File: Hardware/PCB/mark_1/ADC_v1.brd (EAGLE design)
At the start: 52.1 x 49.5 mm, 18 parts, among them IC1 MCP3424, IC2 MCP23017SO, Q1 IRLML6402, Q2 IRLML6402, Q3 IRLML6402, Q4 IRLML6402

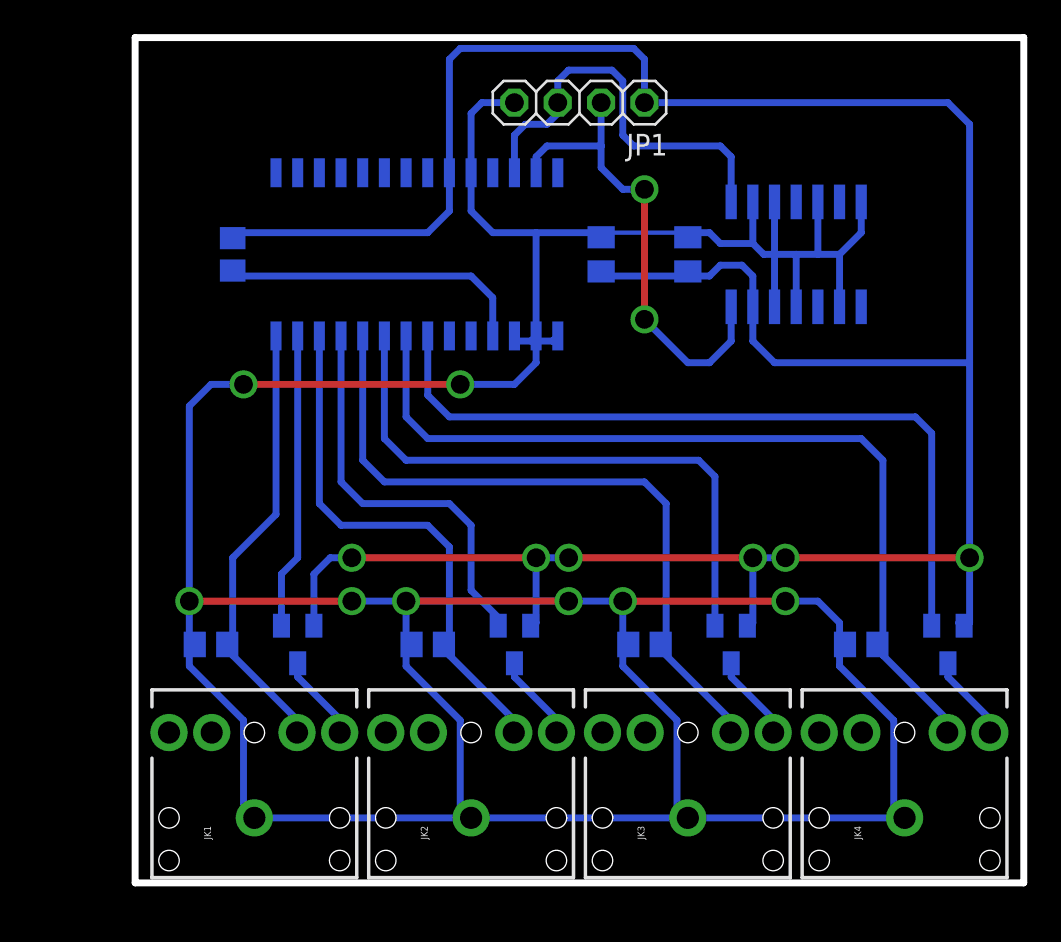
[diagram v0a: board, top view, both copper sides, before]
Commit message: 
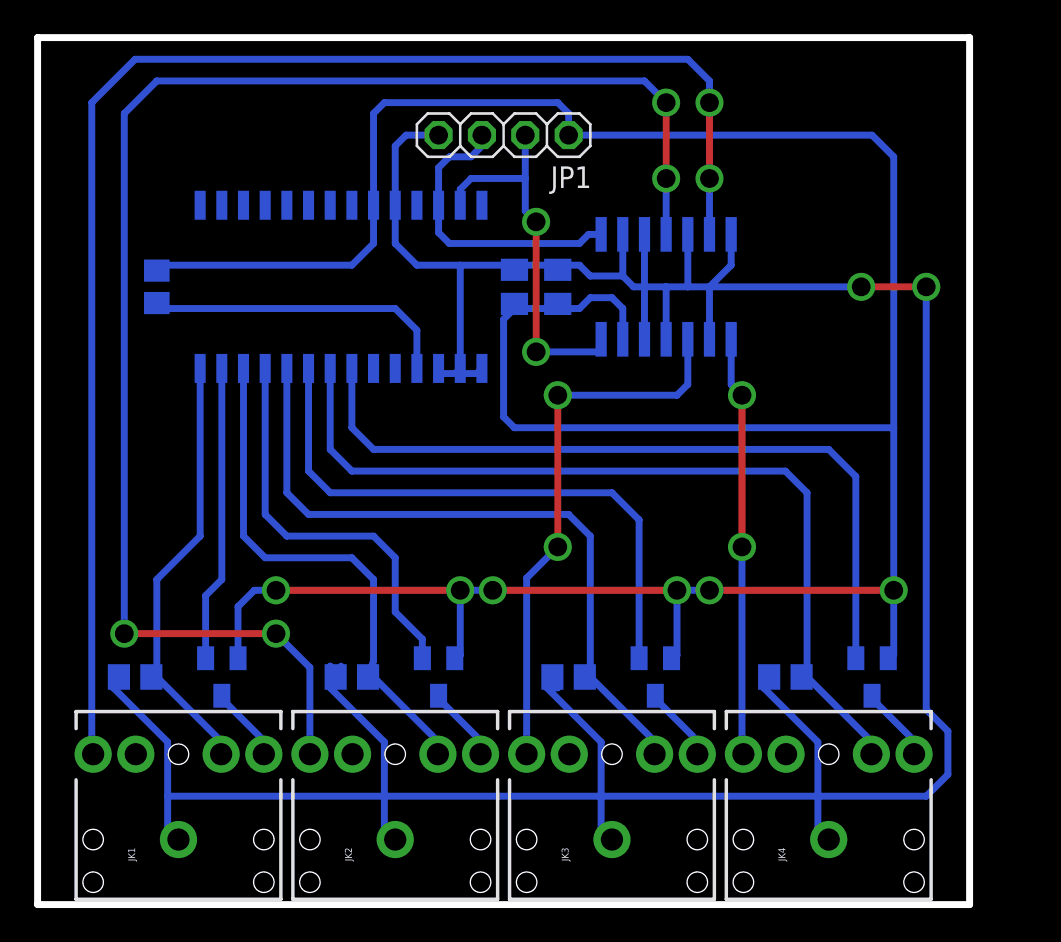
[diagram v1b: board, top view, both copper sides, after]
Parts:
- moved C1 7.85 mm to (29.2, 36.2)
- moved IC1 7.85 mm to (35.6, 36.2)
- moved C2 5.43 mm to (26.7, 36.2)
- moved IC2 4.84 mm to (15.9, 36.2)
- moved JP1 4.84 mm to (26.0, 45.1)
- moved Q1 4.84 mm to (9.53, 13.3)
- moved Q2 4.84 mm to (22.2, 13.3)
- moved Q3 4.84 mm to (34.9, 13.3)
- moved Q4 4.84 mm to (47.6, 13.3)
- moved R1 4.84 mm to (4.45, 13.3)
- moved R2 4.84 mm to (17.1, 13.3)
- moved R3 4.84 mm to (29.8, 13.3)
- moved R4 4.84 mm to (42.5, 13.3)
- moved R5 4.84 mm to (5.71, 36.2)
- moved JK2 4.62 mm to (19.7, 3.81)
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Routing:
- net CH2: track 0.00 -> 88.0 mm, vias 0 -> 4
- net CH1: track 0.00 -> 85.5 mm, vias 0 -> 2
- net GND: track 243.0 -> 198.9 mm, vias 8 -> 2
- net CH3: track 0.00 -> 32.3 mm, vias 0 -> 2
- net CH4: track 0.00 -> 24.6 mm, vias 0 -> 2
- net +5V: track 163.9 -> 172.9 mm
- net SCL: track 24.2 -> 17.5 mm
- net SDA: track 28.2 -> 22.5 mm
- net SN3: track 42.0 -> 40.9 mm
- net N$1: track 5.15 -> 4.51 mm
- net N$5: track 5.15 -> 4.51 mm
- net N$3: track 5.15 -> 4.51 mm
- net N$4: track 5.15 -> 4.51 mm
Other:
- board size 52.1 x 49.5 mm -> 54.6 x 50.8 mm

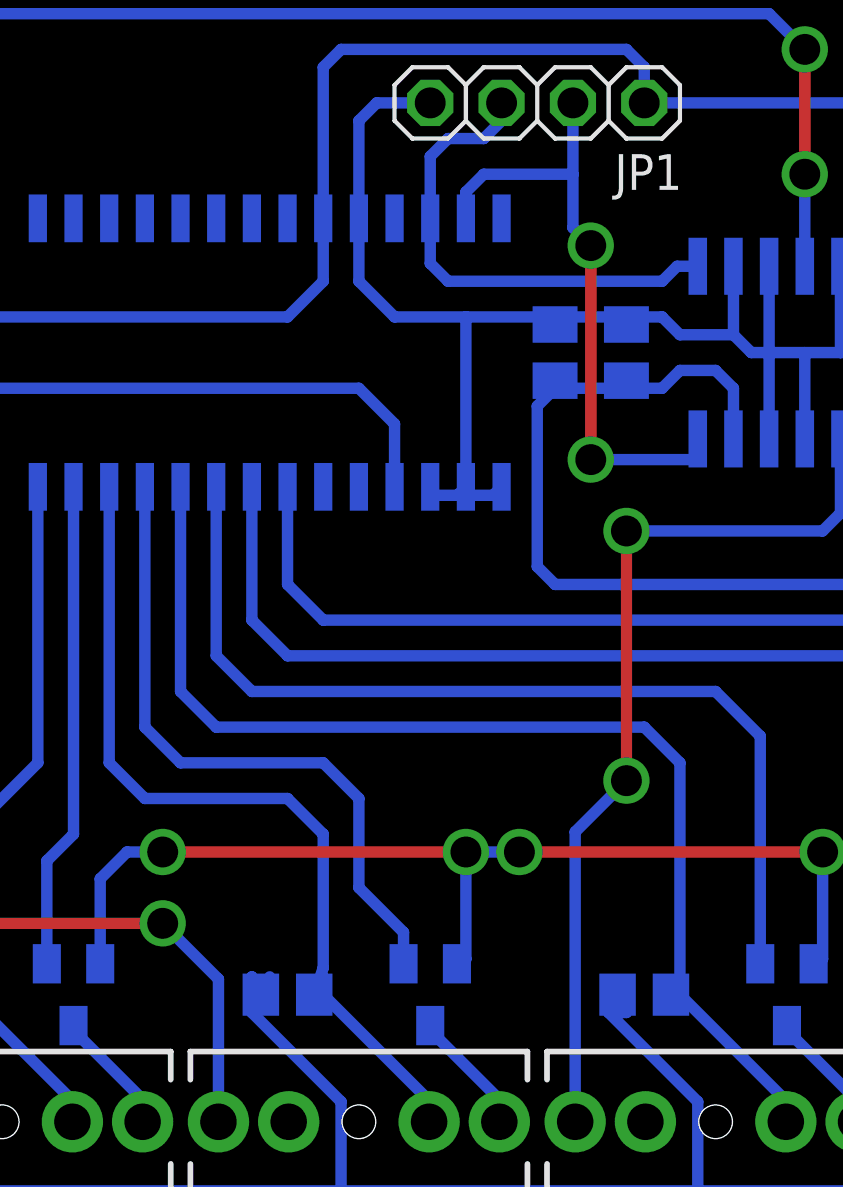
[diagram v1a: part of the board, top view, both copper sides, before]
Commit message: 
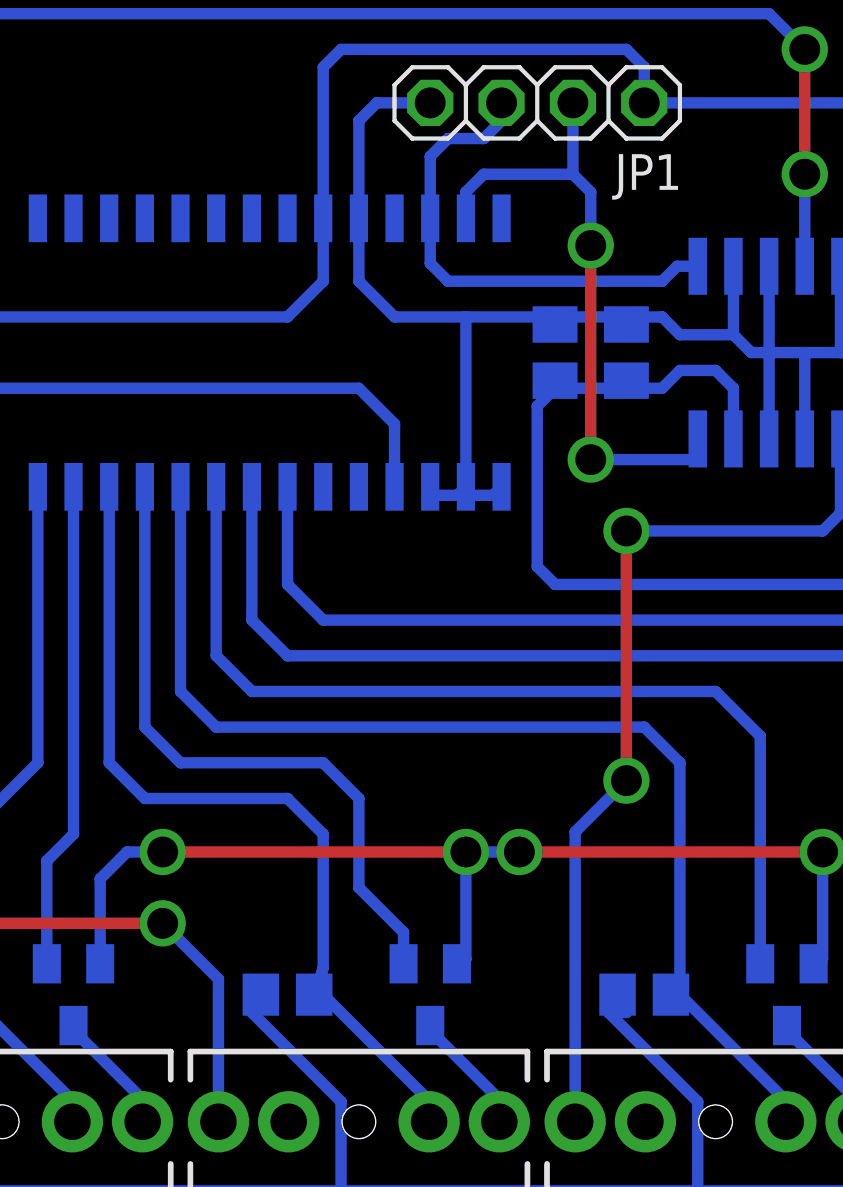
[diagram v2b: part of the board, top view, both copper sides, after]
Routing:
- net GND: track 198.9 -> 197.0 mm
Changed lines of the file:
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@@
 <wire x1="3.495" y1="13.335" x2="3.175" y2="13.335" width="0.4064" layer="16"/>
 <wire x1="19.05" y1="9.525" x2="15.875" y2="12.7" width="0.4064" layer="16"/>
-<wire x1="15.875" y1="12.7" x2="15.875" y2="13.97" width="0.4064" layer="16"/>
-<wire x1="16.195" y1="13.335" x2="16.51" y2="13.97" width="0.4064" layer="16"/>
-<wire x1="15.875" y1="13.97" x2="16.195" y2="13.335" width="0.4064" layer="16"/>
 <wire x1="32.385" y1="3.81" x2="31.75" y2="4.445" width="0.4064" layer="16"/>
 <wire x1="31.75" y1="4.445" x2="31.75" y2="6.35" width="0.4064" layer="16"/>
@@
 <wire x1="41.275" y1="12.7" x2="41.275" y2="13.335" width="0.4064" layer="16"/>
 <wire x1="41.275" y1="13.335" x2="41.595" y2="13.335" width="0.4064" layer="16"/>
-<wire x1="34.29" y1="36.195" x2="35.56" y2="36.195" width="0.4064" layer="16"/>
 <wire x1="35.56" y1="36.195" x2="36.83" y2="36.195" width="0.4064" layer="16"/>
 <wire x1="36.83" y1="36.195" x2="38.1" y2="36.195" width="0.4064" layer="16"/>
@@
 <wire x1="34.29" y1="39.2684" x2="34.29" y2="36.195" width="0.4064" layer="16"/>
 <wire x1="34.29" y1="33.1216" x2="34.29" y2="36.195" width="0.4064" layer="16"/>
-<wire x1="35.56" y1="33.1216" x2="35.56" y2="36.195" width="0.4064" layer="16"/>
 <wire x1="38.1" y1="33.1216" x2="38.1" y2="36.195" width="0.4064" layer="16"/>
 <wire x1="39.37" y1="39.2684" x2="39.37" y2="37.465" width="0.4064" layer="16"/>
@@
 <wire x1="52.07" y1="7.62" x2="50.8" y2="6.35" width="0.4064" layer="16"/>
 <wire x1="50.8" y1="6.35" x2="44.45" y2="6.35" width="0.4064" layer="16"/>
+<wire x1="35.56" y1="33.1216" x2="35.56" y2="36.195" width="0.4064" layer="16"/>
+<wire x1="34.29" y1="36.195" x2="35.56" y2="36.195" width="0.4064" layer="16"/>
+<wire x1="15.875" y1="12.7" x2="15.875" y2="13.015" width="0.4064" layer="16"/>
+<wire x1="15.875" y1="13.015" x2="16.195" y2="13.335" width="0.4064" layer="16"/>
 </signal>
 <signal name="CH1">
@@
 <wire x1="27.94" y1="32.385" x2="27.94" y2="40.005" width="0.4064" layer="1"/>
 <via x="27.94" y="40.005" extent="1-16" drill="1.1" shape="square"/>
-<wire x1="27.94" y1="40.005" x2="27.305" y2="40.64" width="0.4064" layer="16"/>
-<wire x1="27.305" y1="40.64" x2="27.305" y2="42.545" width="0.4064" layer="16"/>
 <wire x1="31.75" y1="32.385" x2="27.94" y2="32.385" width="0.4064" layer="16"/>
+<wire x1="27.94" y1="40.005" x2="27.94" y2="41.91" width="0.4064" layer="16"/>
+<wire x1="27.94" y1="41.91" x2="27.305" y2="42.545" width="0.4064" layer="16"/>
 </signal>
 <signal name="SCL">

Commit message: 
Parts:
- IC2: value MCP23017SO -> MCP23017
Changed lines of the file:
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@@
 </element>
 <element name="C1" library="mark_1" package="C0805K" value="" x="29.21" y="36.195" rot="MR90"/>
-<element name="IC2" library="mark_1" package="SO28W" value="MCP23017SO" x="15.875" y="36.195" rot="MR180">
+<element name="IC2" library="mark_1" package="SO28W" value="MCP23017" x="15.875" y="36.195" rot="MR180">
 <attribute name="OC_NEWARK" value="31K2958" x="41.275" y="42.545" size="1.778" layer="28" rot="MR180" display="off"/>
 <attribute name="MPN" value="MCP23017-E/SO" x="41.275" y="42.545" size="1.778" layer="28" rot="MR180" display="off"/>
